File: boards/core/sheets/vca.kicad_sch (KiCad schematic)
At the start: 24 parts, among them Q202 BC847BS, U207 TL072

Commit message: Added schematics docs
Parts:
- renumbered TP206 to TP202
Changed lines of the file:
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@@
 		(on_board yes)
 		(dnp no)
-		(property "Reference" "TP206"
+		(property "Reference" "TP202"
 			(at 148.59 102.235 90)
 			(effects
@@
 		(on_board yes)
 		(dnp no)
-		(property "Reference" "TP206"
+		(property "Reference" "TP202"
 			(at 158.75 127.635 90)
 			(effects

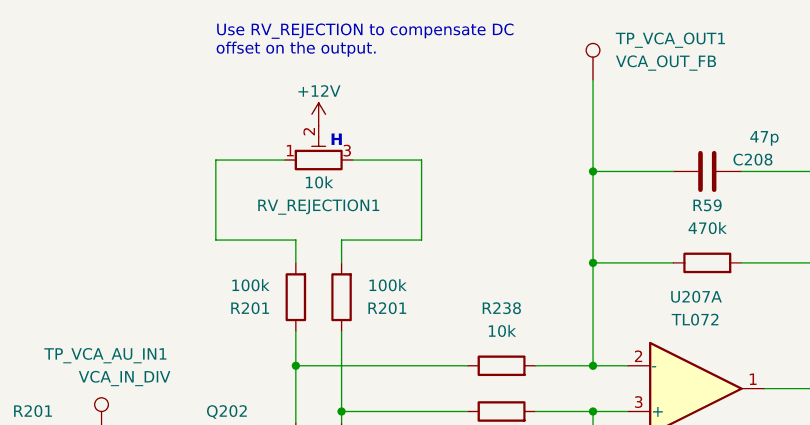
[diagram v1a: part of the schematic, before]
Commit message: Removed VCA rejection trimpot
https://github.com/shmoergh/hog/issues/8

Also updated Core board footprints to work with fcking KiCad 8
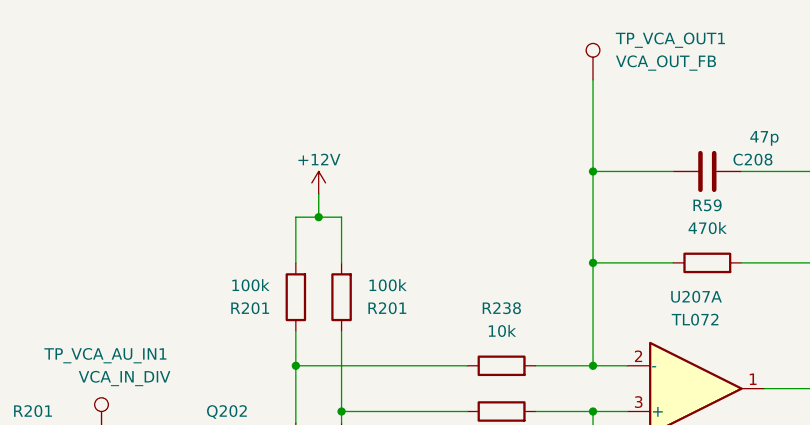
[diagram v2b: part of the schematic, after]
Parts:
- removed RV_REJECTION1: 10k, Potentiometer_THT:Potentiometer_Bourns_3006P_Horizontal, symbol Device:R_Potentiometer_Trim
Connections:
- net +12V: now also R201.2, R201.2
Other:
- note removed: "H"
- note removed: "Use RV_REJECTION to compensate DC offset on the output."
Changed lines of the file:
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@@
+	)
+	(junction
+		(at 154.94 59.69)
+		(diameter 0)
+		(color 0 0 0 0)
 	)
 	(junction
@@
 	(wire
 		(pts
-			(xy 157.48 64.77) (xy 157.48 62.23)
-		)
-		(stroke
-			(width 0)
-			(type default)
-		)
-	)
-	(wire
-		(pts
 			(xy 134.62 107.95) (xy 144.78 107.95)
 		)
@@
 	(wire
 		(pts
+			(xy 152.4 59.69) (xy 154.94 59.69)
+		)
+		(stroke
+			(width 0)
+			(type default)
+		)
+	)
+	(wire
+		(pts
 			(xy 201.93 54.61) (xy 210.82 54.61)
 		)
@@
 	(wire
 		(pts
+			(xy 152.4 59.69) (xy 152.4 64.77)
+		)
+		(stroke
+			(width 0)
+			(type default)
+		)
+	)
+	(wire
+		(pts
 			(xy 130.81 87.63) (xy 144.78 87.63)
 		)
@@
 	(wire
 		(pts
+			(xy 154.94 59.69) (xy 154.94 57.15)
+		)
+		(stroke
+			(width 0)
+			(type default)
+		)
+	)
+	(wire
+		(pts
 			(xy 24.13 167.64) (xy 24.13 168.91)
 		)
@@
 	(wire
 		(pts
-			(xy 151.13 53.34) (xy 143.51 53.34)
-		)
-		(stroke
-			(width 0)
-			(type default)
-		)
-	)
-	(wire
-		(pts
 			(xy 115.57 107.95) (xy 115.57 119.38)
 		)
@@
 	(wire
 		(pts
+			(xy 157.48 59.69) (xy 157.48 64.77)
+		)
+		(stroke
+			(width 0)
+			(type default)
+		)
+	)
+	(wire
+		(pts
 			(xy 157.48 81.28) (xy 171.45 81.28)
 		)
@@
 	(wire
 		(pts
-			(xy 143.51 53.34) (xy 143.51 62.23)
-		)
-		(stroke
-			(width 0)
-			(type default)
-		)
-	)
-	(wire
-		(pts
 			(xy 210.82 64.77) (xy 210.82 78.74)
 		)
@@
 	(wire
 		(pts
-			(xy 166.37 53.34) (xy 166.37 62.23)
-		)
-		(stroke
-			(width 0)
-			(type default)
-		)
-	)
-	(wire
-		(pts
 			(xy 144.78 132.08) (xy 154.94 132.08)
 		)
@@
 	(wire
 		(pts
+			(xy 157.48 59.69) (xy 154.94 59.69)
+		)
+		(stroke
+			(width 0)
+			(type default)
+		)
+	)
+	(wire
+		(pts
 			(xy 179.07 76.2) (xy 185.42 76.2)
 		)
@@
 	(wire
 		(pts
-			(xy 158.75 53.34) (xy 166.37 53.34)
-		)
-		(stroke
-			(width 0)
-			(type default)
-		)
-	)
-	(wire
-		(pts
-			(xy 143.51 62.23) (xy 152.4 62.23)
-		)
-		(stroke
-			(width 0)
-			(type default)
-		)
-	)
-	(wire
-		(pts
 			(xy 123.19 134.62) (xy 125.73 134.62)
 		)
@@
 	(wire
 		(pts
-			(xy 152.4 62.23) (xy 152.4 64.77)
-		)
-		(stroke
-			(width 0)
-			(type default)
-		)
-	)
-	(wire
-		(pts
 			(xy 105.41 87.63) (xy 111.76 87.63)
 		)
@@
 	(wire
 		(pts
-			(xy 157.48 62.23) (xy 166.37 62.23)
-		)
-		(stroke
-			(width 0)
-			(type default)
-		)
-	)
-	(wire
-		(pts
 			(xy 123.19 134.62) (xy 123.19 138.43)
 		)
@@
 			(width 0)
 			(type default)
-		)
-	)
-	(text "H"
-		(exclude_from_sim no)
-		(at 156.21 52.07 0)
-		(effects
-			(font
-				(size 1.27 1.27)
-				(thickness 0.254)
-				(bold yes)
-				(color 255 0 221 1)
-			)
-			(justify left bottom)
 		)
 	)
@@
 		(exclude_from_sim no)
 		(at 77.47 115.57 0)
-		(effects
-			(font
-				(size 1.27 1.27)
-			)
-			(justify left bottom)
-		)
-	)
-	(text "Use RV_REJECTION to compensate DC \noffset on the output."
-		(exclude_from_sim no)
-		(at 143.51 41.91 0)
 		(effects
 			(font
@@
 		(lib_name "+12V_1")
 		(lib_id "power:+12V")
-		(at 154.94 49.53 0)
+		(at 154.94 57.15 0)
 		(unit 1)
 		(exclude_from_sim no)
@@
 		(fields_autoplaced yes)
 		(property "Reference" "#PWR0110"
+			(at 154.94 60.96 0)
+			(effects
+				(font
+					(size 1.27 1.27)
+				)
+				(hide yes)
+			)
+		)
+		(property "Value" "+12V"
 			(at 154.94 53.34 0)
 			(effects
@@
 					(size 1.27 1.27)
 				)
-				(hide yes)
-			)
-		)
-		(property "Value" "+12V"
-			(at 154.94 45.72 0)
-			(effects
-				(font
-					(size 1.27 1.27)
-				)
 			)
 		)
 		(property "Footprint" ""
-			(at 154.94 49.53 0)
+			(at 154.94 57.15 0)
 			(effects
 				(font
@@
 		)
 		(property "Datasheet" ""
-			(at 154.94 49.53 0)
+			(at 154.94 57.15 0)
 			(effects
 				(font
@@
 		)
 		(property "Description" ""
-			(at 154.94 49.53 0)
+			(at 154.94 57.15 0)
 			(effects
 				(font
@@
 					(unit 1)
 				)
-			)
-		)
-	)
-	(symbol
-		(lib_id "Device:R_Potentiometer_Trim")
-		(at 154.94 53.34 90)
-		(unit 1)
-		(exclude_from_sim no)
-		(in_bom no)
-		(on_board yes)
-		(dnp no)
-		(property "Reference" "RV_REJECTION1"
-			(at 154.94 58.42 90)
-			(effects
-				(font
-					(size 1.27 1.27)
-				)
-			)
-		)
-		(property "Value" "10k"
-			(at 154.94 55.88 90)
-			(effects
-				(font
-					(size 1.27 1.27)
-				)
-			)
-		)
-		(property "Footprint" "Potentiometer_THT:Potentiometer_Bourns_3006P_Horizontal"
-			(at 154.94 53.34 0)
-			(effects
-				(font
-					(size 1.27 1.27)
-				)
-				(hide yes)
-			)
-		)
-		(property "Datasheet" "~"
-			(at 154.94 53.34 0)
-			(effects
-				(font
-					(size 1.27 1.27)
-				)
-				(hide yes)
-			)
-		)
-		(property "Description" ""
-			(at 154.94 53.34 0)
-			(effects
-				(font
-					(size 1.27 1.27)
-				)
-				(hide yes)
-			)
-		)
-		(pin "1"
-		)
-		(pin "2"
-		)
-		(pin "3"
-		)
-		(instances
-			(project "shmoergh-funk-live-control"
-				(path "/6d7b782d-8b2e-4b40-a99f-4bf41187d978/6b0f1c86-305d-46a4-9f99-ea8eed307ff5"
-					(reference "RV_REJECTION1")
-					(unit 1)
-				)
-			)
-			(project "core-rev-3"
-				(path "/91ae1fff-f2ac-4868-8c3f-8c5c03d8b2f6/dca47c1e-77dc-4eaf-bf96-31f48abca153"
-					(reference "RV_VCA_REJECTION201")
-					(unit 1)
-				)
